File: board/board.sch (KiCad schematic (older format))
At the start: 47 parts, among them Q1 AO3401A, U1 STM32F405RGTx, U2 TPS542941, U3 MX25R3235FM2xx1, Y1 16MHz

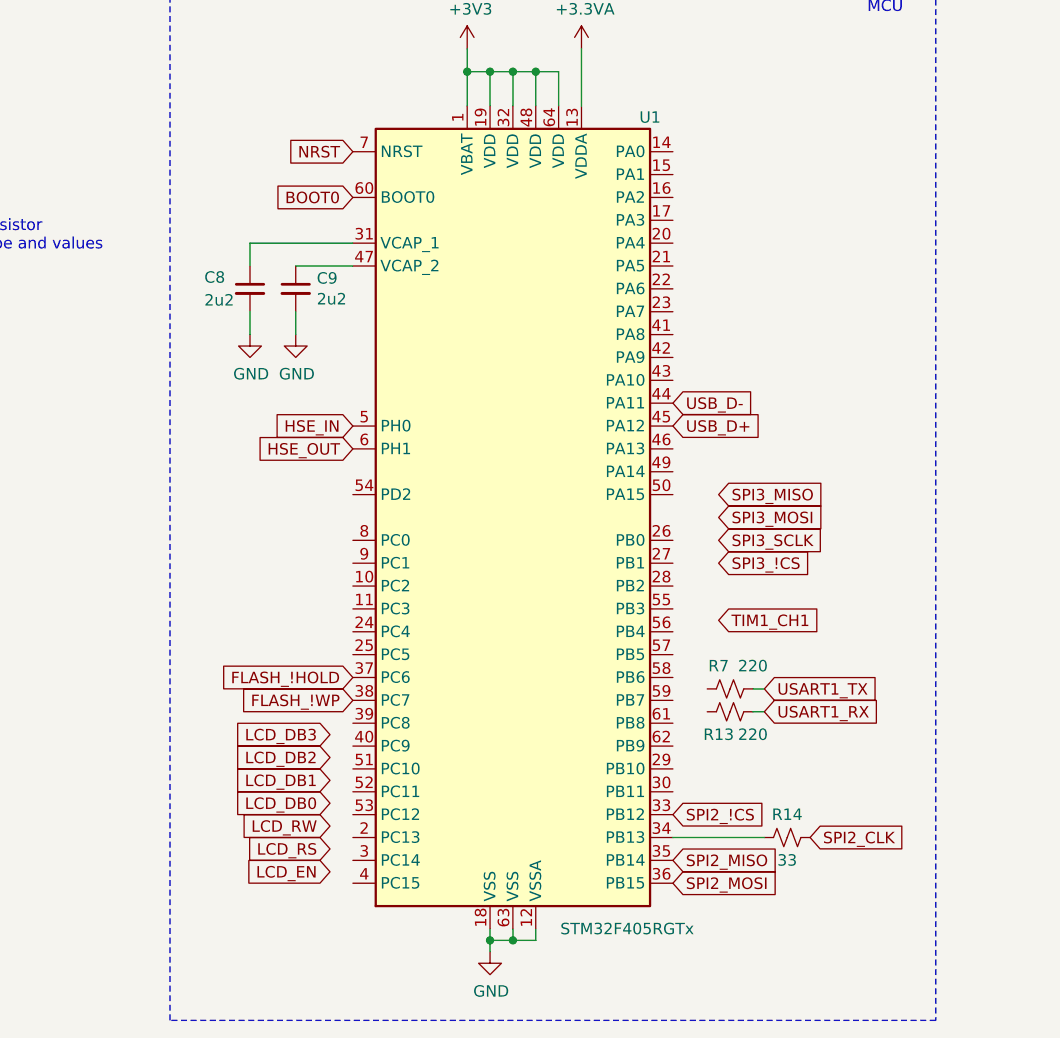
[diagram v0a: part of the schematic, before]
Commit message: Update on pinout
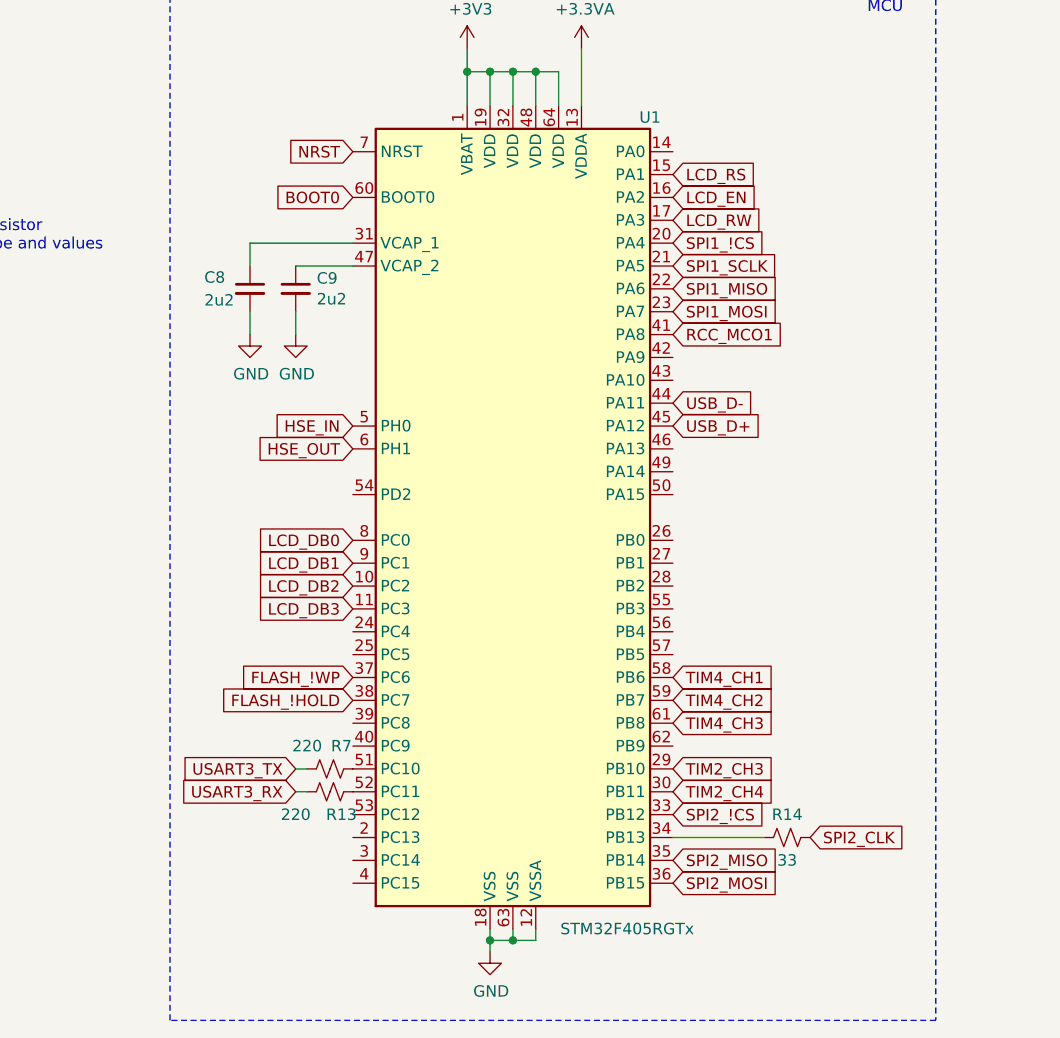
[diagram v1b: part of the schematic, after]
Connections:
- net FLASH_!HOLD: now also U1.38 (PC7); no longer U1.37 (PC6)
- net FLASH_!WP: now also U1.37 (PC6); no longer U1.38 (PC7)
- net LCD_DB0: now also U1.8 (PC0)
- net LCD_DB1: now also U1.9 (PC1)
- net LCD_DB2: now also U1.10 (PC2)
- net LCD_DB3: now also U1.11 (PC3)
- net LCD_EN: now also U1.16 (PA2)
- net LCD_RS: now also U1.15 (PA1)
- net LCD_RW: now also U1.17 (PA3)
- net SPI1_!CS: now reaches U1.20 (PA4)
- net SPI1_SCLK: now reaches U1.21 (PA5)
- net SPI1_MISO: now reaches U1.22 (PA6)
- net SPI1_MOSI: now reaches U1.23 (PA7)
- net TIM2_CH3: now reaches U1.29 (PB10)
- net TIM2_CH4: now reaches U1.30 (PB11)
- net RCC_MCO1: now reaches U1.41 (PA8)
- net at U1.51 (PC10): now also R7.2
- net at U1.52 (PC11): now also R13.2
- net TIM4_CH1: now reaches U1.58 (PB6)
- net TIM4_CH2: now reaches U1.59 (PB7)
- net TIM4_CH3: now reaches U1.61 (PB8)
- net USART1_RX renamed USART3_RX
- net USART1_TX renamed USART3_TX
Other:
- moved on the sheet: R13, R7
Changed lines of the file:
@@
 Text GLabel 4150 7000 2    50   Input ~ 0
 SPI2_MOSI
+Text GLabel 2750 6200 0    50   Input ~ 0
+FLASH_!HOLD
 Text GLabel 2750 6100 0    50   Input ~ 0
-FLASH_!HOLD
-Text GLabel 2750 6200 0    50   Input ~ 0
 FLASH_!WP
 Text GLabel 4150 6900 2    50   Input ~ 0
@@
 F1 "sensors.sch" 50
 $EndSheet
-Text GLabel 4350 5850 2    50   Input ~ 0
-TIM1_CH1
 $Sheet
 S 2950 -1250 1300 900
@@
 F1 "connectors.sch" 50
 $EndSheet
-Text GLabel 4350 5600 2    50   Input ~ 0
-SPI3_!CS
-Text GLabel 4350 5500 2    50   Input ~ 0
-SPI3_SCLK
-Text GLabel 4350 5400 2    50   Input ~ 0
-SPI3_MOSI
-Text GLabel 4350 5300 2    50   Input ~ 0
-SPI3_MISO
+Text GLabel 4150 4200 2    50   Input ~ 0
+SPI1_!CS
+Text GLabel 4150 4300 2    50   Input ~ 0
+SPI1_SCLK
+Text GLabel 4150 4500 2    50   Input ~ 0
+SPI1_MOSI
+Text GLabel 4150 4400 2    50   Input ~ 0
+SPI1_MISO
 Wire Notes Line
 	3700 600  3700 1500
 Wire Notes Line
 	5450 1500 5450 600
-Text GLabel 4550 6150 2    50   Input ~ 0
-USART1_TX
-Text GLabel 4550 6250 2    50   Input ~ 0
-USART1_RX
-Text GLabel 2650 6950 0    50   Input ~ 0
+Text GLabel 4150 4000 2    50   Input ~ 0
 LCD_EN
-Text GLabel 2650 6750 0    50   Input ~ 0
+Text GLabel 4150 4100 2    50   Input ~ 0
 LCD_RW
 $Comp
@@
 	1    0    0    -1
 $EndComp
-Text GLabel 2650 6650 0    50   Input ~ 0
+Text GLabel 2750 5500 0    50   Input ~ 0
 LCD_DB0
-Text GLabel 2650 6550 0    50   Input ~ 0
+Text GLabel 2750 5600 0    50   Input ~ 0
 LCD_DB1
-Text GLabel 2650 6450 0    50   Input ~ 0
+Text GLabel 2750 5700 0    50   Input ~ 0
 LCD_DB2
-Text GLabel 2650 6350 0    50   Input ~ 0
+Text GLabel 2750 5800 0    50   Input ~ 0
 LCD_DB3
-Text GLabel 2650 6850 0    50   Input ~ 0
+Text GLabel 4150 3900 2    50   Input ~ 0
 LCD_RS
 $Comp
@@
 	6700 2800 6700 6250
 Wire Notes Line
-	5300 3050 5300 7600
-Wire Notes Line
 	5300 7600 1950 7600
 Wire Notes Line
@@
 Text Notes 2800 700  0    50   ~ 0
 MCU PWR Decoupling\n
+NoConn ~ 9250 5600
+NoConn ~ 8400 5600
+Text GLabel 4150 6500 2    50   Input ~ 0
+TIM2_CH3
+Text GLabel 4150 6600 2    50   Input ~ 0
+TIM2_CH4
+Text GLabel 4150 6100 2    50   Input ~ 0
+TIM4_CH1
+Text GLabel 4150 6200 2    50   Input ~ 0
+TIM4_CH2
+Text GLabel 4150 6300 2    50   Input ~ 0
+TIM4_CH3
+Wire Wire Line
+	2500 6600 2550 6600
+Wire Wire Line
+	2500 6500 2550 6500
+$Comp
+L Device:R_Small_US R13
+U 1 1 60B24566
+P 2650 6600
+F 0 "R13" V 2550 6550 50  0000 C CNN
+F 1 "220" V 2550 6750 50  0000 C CNN
+F 2 "Resistor_SMD:R_0603_1608Metric" H 2650 6600 50  0001 C CNN
+F 3 "~" H 2650 6600 50  0001 C CNN
+	1    2650 6600
+	0    -1   -1   0
+$EndComp
 $Comp
 L Device:R_Small_US R7
 U 1 1 60B240EB
-P 4400 6150
-F 0 "R7" V 4300 6100 50  0000 C CNN
-F 1 "220" V 4300 6250 50  0000 C CNN
-F 2 "Resistor_SMD:R_0603_1608Metric" H 4400 6150 50  0001 C CNN
-F 3 "~" H 4400 6150 50  0001 C CNN
-	1    4400 6150
-	0    1    1    0
-$EndComp
-$Comp
-L Device:R_Small_US R13
-U 1 1 60B24566
-P 4400 6250
-F 0 "R13" V 4500 6200 50  0000 C CNN
-F 1 "220" V 4500 6350 50  0000 C CNN
-F 2 "Resistor_SMD:R_0603_1608Metric" H 4400 6250 50  0001 C CNN
-F 3 "~" H 4400 6250 50  0001 C CNN
-	1    4400 6250
-	0    1    1    0
-$EndComp
-Wire Wire Line
-	4550 6150 4500 6150
-Wire Wire Line
-	4550 6250 4500 6250
-NoConn ~ 9250 5600
-NoConn ~ 8400 5600
+P 2650 6500
+F 0 "R7" V 2750 6450 50  0000 C CNN
+F 1 "220" V 2750 6600 50  0000 C CNN
+F 2 "Resistor_SMD:R_0603_1608Metric" H 2650 6500 50  0001 C CNN
+F 3 "~" H 2650 6500 50  0001 C CNN
+	1    2650 6500
+	0    -1   -1   0
+$EndComp
+Wire Notes Line
+	5300 3050 5300 7600
+Text GLabel 2500 6600 0    50   Input ~ 0
+USART3_RX
+Text GLabel 2500 6500 0    50   Input ~ 0
+USART3_TX
+Text GLabel 4150 4600 2    50   Input ~ 0
+RCC_MCO1
 $EndSCHEMATC

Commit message: Updated schematic
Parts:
- removed C18: 100n, Capacitor_SMD:C_0402_1005Metric, symbol Device:C_Small
- removed R14: 33, Resistor_SMD:R_0603_1608Metric, symbol Device:R_Small_US
- removed R15, R3, R6: 10k, Resistor_SMD:R_0603_1608Metric, symbol Device:R_Small_US
- removed U3: MX25R3235FM2xx1, Package_SO:SOP-8_5.28x5.23mm_P1.27mm, symbol Memory_Flash:MX25R3235FM2xx1
- added C19: 10u, Capacitor_SMD:C_0603_1608Metric, symbol Device:C_Small
- added D2: LED_RGB, symbol Device:LED_RGB
- added Q2, Q3, Q4: Q_NMOS_GDS, symbol Device:Q_NMOS_GDS
- added R7: 220, Resistor_SMD:R_0603_1608Metric, symbol Device:R_Small_US
- added R8, R9: 120, Resistor_SMD:R_0603_1608Metric, symbol Device:R_Small_US
- renumbered C24 to C11, C25 to C12, C26 to C13, C11 to C14, C13 to C15, C14 to C16, C12 to C17, C15 to C18, C8 to C2, C16 to C20, C17 to C21, C19 to C22, C20 to C23, C21 to C24, C9 to C4, C2 to C5, C5 to C6, C4 to C7, C6 to C8, C7 to C9, R7 to R1, R8 to R10, R9 to R11, R13 to R2, R1 to R3, R2 to R4, R4 to R5, R5 to R6
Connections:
- net labels added: 12V_IN, SPI1_CLK
- net labels removed: +12V, SPI1_SCLK
- wire segments 141 -> 149
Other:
- note added: "Connectors"
- note added: "Flush Surveillance Concept"
- note added: "RGB"
- note added: "Sensors"
- note added: "UART series resistor\nDecoupling type and values"
- note removed: "Check if this is pull up or down"
- note removed: "Custom STM32 Board"
- note removed: "Ext. Flash"
- note removed: "UART series resistor\nDecoupling type and values\nLCD ??\nPower LED???"
- note removed: "Under construction"
- moved on the sheet: C1, C10, C11, C12, C13, C14, C15, C16, C17, C18, C2, C20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

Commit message: Updated schematic
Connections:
- net labels added: +12V
- net labels removed: 12V_IN
- wire segments 149 -> 150
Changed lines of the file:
@@
 Wire Notes Line
 	6200 650  4500 650
-Wire Wire Line
-	4850 2100 4900 2100
-Text GLabel 4850 2100 0    50   Input ~ 0
-12V_IN
 NoConn ~ 6200 4450
 NoConn ~ 7050 4450
@@
 Text Notes 1400 -1400 0    98   ~ 20
 Sensors
+$Comp
+L power:+12V #PWR?
+U 1 1 60B83527
+P 4800 1950
+F 0 "#PWR?" H 4800 1800 50  0001 C CNN
+F 1 "+12V" H 4815 2123 50  0000 C CNN
+F 2 "" H 4800 1950 50  0001 C CNN
+F 3 "" H 4800 1950 50  0001 C CNN
+	1    4800 1950
+	1    0    0    -1
+$EndComp
+Wire Wire Line
+	4800 1950 4800 2100
+Wire Wire Line
+	4800 2100 4900 2100
 $EndSCHEMATC

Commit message: Updated footprints
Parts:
- D2: footprint (none) -> LED_SMD:LED_RGB_1210
- Q2, Q3, Q4: footprint (none) -> Package_TO_SOT_SMD:SOT-23
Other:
- note added: "Find RGB\n"
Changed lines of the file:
@@
 F 0 "Q2" H 5400 6700 50  0000 L CNN
 F 1 "Q_NMOS_GDS" H 5100 6600 50  0000 L CNN
-F 2 "" H 5400 6650 50  0001 C CNN
+F 2 "Package_TO_SOT_SMD:SOT-23" H 5400 6650 50  0001 C CNN
 F 3 "~" H 5200 6550 50  0001 C CNN
 	1    5200 6550
@@
 F 0 "Q3" H 5804 6896 50  0000 L CNN
 F 1 "Q_NMOS_GDS" H 5804 6805 50  0000 L CNN
-F 2 "" H 5800 6950 50  0001 C CNN
+F 2 "Package_TO_SOT_SMD:SOT-23" H 5800 6950 50  0001 C CNN
 F 3 "~" H 5600 6850 50  0001 C CNN
 	1    5600 6850
@@
 F 0 "Q4" H 6250 6700 50  0000 L CNN
 F 1 "Q_NMOS_GDS" H 6250 6600 50  0000 L CNN
-F 2 "" H 6250 6650 50  0001 C CNN
+F 2 "Package_TO_SOT_SMD:SOT-23" H 6250 6650 50  0001 C CNN
 F 3 "~" H 6050 6550 50  0001 C CNN
 	1    6050 6550
@@
 	6150 5550 6100 5550
 $Comp
-L power:GND #PWR021
+L power:GND #PWR022
 U 1 1 60BEDB34
 P 6150 5550
-F 0 "#PWR021" H 6150 5300 50  0001 C CNN
+F 0 "#PWR022" H 6150 5300 50  0001 C CNN
 F 1 "GND" H 6155 5377 50  0000 C CNN
 F 2 "" H 6150 5550 50  0001 C CNN
@@
 	5700 5550 5700 5650
 $Comp
-L power:+3V3 #PWR019
+L power:+3V3 #PWR020
 U 1 1 60BE178F
 P 5700 5500
-F 0 "#PWR019" H 5700 5350 50  0001 C CNN
+F 0 "#PWR020" H 5700 5350 50  0001 C CNN
 F 1 "+3V3" H 5715 5673 50  0000 C CNN
 F 2 "" H 5700 5500 50  0001 C CNN
@@
 $EndComp
 $Comp
-L power:GND #PWR020
+L power:GND #PWR021
 U 1 1 60BE0B31
 P 5700 7200
-F 0 "#PWR020" H 5700 6950 50  0001 C CNN
+F 0 "#PWR021" H 5700 6950 50  0001 C CNN
 F 1 "GND" H 5850 7150 50  0000 C CNN
 F 2 "" H 5700 7200 50  0001 C CNN
@@
 F 0 "D2" V 5746 5520 50  0000 R CNN
 F 1 "LED_RGB" V 5655 5520 50  0000 R CNN
-F 2 "" H 5700 5800 50  0001 C CNN
+F 2 "LED_SMD:LED_RGB_1210" H 5700 5800 50  0001 C CNN
 F 3 "~" H 5700 5800 50  0001 C CNN
 	1    5700 5850
@@
 	5050 3200 5050 3250
 $Comp
-L power:GND #PWR023
+L power:GND #PWR024
 U 1 1 60B1C138
 P 7150 4950
-F 0 "#PWR023" H 7150 4700 50  0001 C CNN
+F 0 "#PWR024" H 7150 4700 50  0001 C CNN
 F 1 "GND" H 7000 4900 50  0000 C CNN
 F 2 "" H 7150 4950 50  0001 C CNN
@@
 VFB2
 $Comp
-L power:GND #PWR026
+L power:GND #PWR027
 U 1 1 60B00D4D
 P 8550 4400
-F 0 "#PWR026" H 8550 4150 50  0001 C CNN
+F 0 "#PWR027" H 8550 4150 50  0001 C CNN
 F 1 "GND" H 8555 4227 50  0000 C CNN
 F 2 "" H 8550 4400 50  0001 C CNN
@@
 EN2_IN
 $Comp
-L power:GND #PWR024
+L power:GND #PWR025
 U 1 1 60AF4CB3
 P 8400 3600
-F 0 "#PWR024" H 8400 3350 50  0001 C CNN
+F 0 "#PWR025" H 8400 3350 50  0001 C CNN
 F 1 "GND" H 8405 3427 50  0000 C CNN
 F 2 "" H 8400 3600 50  0001 C CNN
@@
 PGND1
 $Comp
-L power:GND #PWR016
+L power:GND #PWR017
 U 1 1 60A75B9C
 P 5250 3550
-F 0 "#PWR016" H 5250 3300 50  0001 C CNN
+F 0 "#PWR017" H 5250 3300 50  0001 C CNN
 F 1 "GND" H 5255 3377 50  0000 C CNN
 F 2 "" H 5250 3550 50  0001 C CNN
@@
 $EndComp
 $Comp
-L power:GND #PWR013
+L power:GND #PWR014
 U 1 1 60A78713
 P 5050 4150
-F 0 "#PWR013" H 5050 3900 50  0001 C CNN
+F 0 "#PWR014" H 5050 3900 50  0001 C CNN
 F 1 "GND" H 5055 3977 50  0000 C CNN
 F 2 "" H 5050 4150 50  0001 C CNN
@@
 $EndComp
 $Comp
-L power:+5V #PWR012
+L power:+5V #PWR013
 U 1 1 60A6D9C0
 P 5050 3200
-F 0 "#PWR012" H 5050 3050 50  0001 C CNN
+F 0 "#PWR013" H 5050 3050 50  0001 C CNN
 F 1 "+5V" H 5065 3373 50  0000 C CNN
 F 2 "" H 5050 3200 50  0001 C CNN
@@
 $EndComp
 $Comp
-L power:+3V3 #PWR025
+L power:+3V3 #PWR026
 U 1 1 60A69F8C
 P 8550 3200
-F 0 "#PWR025" H 8550 3050 50  0001 C CNN
+F 0 "#PWR026" H 8550 3050 50  0001 C CNN
 F 1 "+3V3" H 8565 3373 50  0000 C CNN
 F 2 "" H 8550 3200 50  0001 C CNN
@@
 $EndComp
 $Comp
-L power:GND #PWR014
+L power:GND #PWR015
 U 1 1 6090B6B1
 P 5100 2400
-F 0 "#PWR014" H 5100 2150 50  0001 C CNN
+F 0 "#PWR015" H 5100 2150 50  0001 C CNN
 F 1 "GND" H 5105 2227 50  0000 C CNN
 F 2 "" H 5100 2400 50  0001 C CNN
@@
 $EndComp
 $Comp
-L power:GND #PWR022
+L power:GND #PWR023
 U 1 1 60910D18
 P 6300 2300
-F 0 "#PWR022" H 6300 2050 50  0001 C CNN
+F 0 "#PWR023" H 6300 2050 50  0001 C CNN
 F 1 "GND" H 6305 2127 50  0000 C CNN
 F 2 "" H 6300 2300 50  0001 C CNN
@@
 	6200 1550 6200 650
 $Comp
-L power:GND #PWR018
+L power:GND #PWR019
 U 1 1 60A3071E
 P 5600 1250
-F 0 "#PWR018" H 5600 1000 50  0001 C CNN
+F 0 "#PWR019" H 5600 1000 50  0001 C CNN
 F 1 "GND" H 5605 1077 50  0000 C CNN
 F 2 "" H 5600 1250 50  0001 C CNN
@@
 $EndComp
 $Comp
-L power:GND #PWR015
+L power:GND #PWR016
 U 1 1 60A2FFCD
 P 5200 1250
-F 0 "#PWR015" H 5200 1000 50  0001 C CNN
+F 0 "#PWR016" H 5200 1000 50  0001 C CNN
 F 1 "GND" H 5205 1077 50  0000 C CNN
 F 2 "" H 5200 1250 50  0001 C CNN
@@
 	5600 950  5600 1050
 $Comp
-L power:+3.3VA #PWR017
+L power:+3.3VA #PWR018
 U 1 1 60A2600F
 P 5600 950
-F 0 "#PWR017" H 5600 800 50  0001 C CNN
+F 0 "#PWR018" H 5600 800 50  0001 C CNN
 F 1 "+3.3VA" H 5615 1123 50  0000 C CNN
 F 2 "" H 5600 950 50  0001 C CNN
@@
 Sensors
 $Comp
-L power:+12V #PWR?
+L power:+12V #PWR012
 U 1 1 60B83527
 P 4800 1950
-F 0 "#PWR?" H 4800 1800 50  0001 C CNN
+F 0 "#PWR012" H 4800 1800 50  0001 C CNN
 F 1 "+12V" H 4815 2123 50  0000 C CNN
 F 2 "" H 4800 1950 50  0001 C CNN
@@
 Wire Wire Line
 	4800 2100 4900 2100
+Text Notes 6650 5550 0    98   ~ 20
+Find RGB\n
 $EndSCHEMATC

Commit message: Updated layout
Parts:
- removed Q1: AO3401A, Package_TO_SOT_SMD:SOT-23, symbol Transistor_FET:AO3401A
- removed R1, R2: 220, Resistor_SMD:R_0603_1608Metric, symbol Device:R_Small_US
- removed U1: STM32F405RGTx, Package_QFP:LQFP-64_10x10mm_P0.5mm, symbol MCU_ST_STM32F4:STM32F405RGTx
- added U?: STM32F405RGTx, Package_QFP:LQFP-64_10x10mm_P0.5mm, symbol MCU_ST_STM32F4:STM32F405RGTx
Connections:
- wire segments 150 -> 147
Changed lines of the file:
@@
 Flush Surveillance Concept
-$Comp
-L MCU_ST_STM32F4:STM32F405RGTx U1
-U 1 1 608D985A
-P 2400 4000
-F 0 "U1" H 3000 5750 50  0000 C CNN
-F 1 "STM32F405RGTx" H 2900 2200 50  0000 C CNN
-F 2 "Package_QFP:LQFP-64_10x10mm_P0.5mm" H 1800 2300 50  0001 R CNN
-F 3 "http://www.st.com/st-web-ui/static/active/en/resource/technical/document/datasheet/DM00037051.pdf" H 2400 4000 50  0001 C CNN
-	1    2400 4000
-	1    0    0    -1
-$EndComp
 $Comp
 L power:+3V3 #PWR06
@@
 Text GLabel 3100 4900 2    50   Input ~ 0
 TIM4_CH3
-Wire Wire Line
-	1450 5200 1500 5200
-Wire Wire Line
-	1450 5100 1500 5100
-$Comp
-L Device:R_Small_US R2
-U 1 1 60B24566
-P 1600 5200
-F 0 "R2" V 1500 5150 50  0000 C CNN
-F 1 "220" V 1500 5350 50  0000 C CNN
-F 2 "Resistor_SMD:R_0603_1608Metric" H 1600 5200 50  0001 C CNN
-F 3 "~" H 1600 5200 50  0001 C CNN
-	1    1600 5200
-	0    -1   -1   0
-$EndComp
-$Comp
-L Device:R_Small_US R1
-U 1 1 60B240EB
-P 1600 5100
-F 0 "R1" V 1700 5050 50  0000 C CNN
-F 1 "220" V 1700 5200 50  0000 C CNN
-F 2 "Resistor_SMD:R_0603_1608Metric" H 1600 5100 50  0001 C CNN
-F 3 "~" H 1600 5100 50  0001 C CNN
-	1    1600 5100
-	0    -1   -1   0
-$EndComp
-Text GLabel 1450 5200 0    50   Input ~ 0
-USART3_RX
-Text GLabel 1450 5100 0    50   Input ~ 0
-USART3_TX
 Text GLabel 3100 3200 2    50   Input ~ 0
 RCC_MCO1
@@
 Wire Wire Line
 	5700 2100 5850 2100
-Wire Wire Line
-	5300 2100 5500 2100
 $Comp
 L board-rescue:TPS542941 U2
@@
 $EndComp
 $Comp
-L Transistor_FET:AO3401A Q1
-U 1 1 60907C55
-P 5100 2200
-F 0 "Q1" V 5442 2200 50  0000 C CNN
-F 1 "AO3401A" V 5351 2200 50  0000 C CNN
-F 2 "Package_TO_SOT_SMD:SOT-23" H 5300 2125 50  0001 L CIN
-F 3 "http://www.aosmd.com/pdfs/datasheet/AO3401A.pdf" H 5100 2200 50  0001 L CNN
-	1    5100 2200
-	0    -1   -1   0
-$EndComp
-$Comp
-L power:GND #PWR015
-U 1 1 6090B6B1
-P 5100 2400
-F 0 "#PWR015" H 5100 2150 50  0001 C CNN
-F 1 "GND" H 5105 2227 50  0000 C CNN
-F 2 "" H 5100 2400 50  0001 C CNN
-F 3 "" H 5100 2400 50  0001 C CNN
-	1    5100 2400
-	1    0    0    -1
-$EndComp
-$Comp
 L Device:Ferrite_Bead_Small FB2
 U 1 1 6090BE99
@@
 Wire Wire Line
 	4800 1950 4800 2100
-Wire Wire Line
-	4800 2100 4900 2100
 Text Notes 6650 5550 0    98   ~ 20
 Find RGB\n
+Text GLabel 1700 5100 0    50   Input ~ 0
+USART3_TX
+Text GLabel 1700 5200 0    50   Input ~ 0
+USART3_RX
+$Comp
+L MCU_ST_STM32F4:STM32F405RGTx U?
+U 1 1 60C86C3C
+P 2400 4000
+F 0 "U?" H 2850 5800 50  0000 C CNN
+F 1 "STM32F405RGTx" H 2950 2150 50  0000 C CNN
+F 2 "Package_QFP:LQFP-64_10x10mm_P0.5mm" H 1800 2300 50  0001 R CNN
+F 3 "http://www.st.com/st-web-ui/static/active/en/resource/technical/document/datasheet/DM00037051.pdf" H 2400 4000 50  0001 C CNN
+	1    2400 4000
+	1    0    0    -1
+$EndComp
+Wire Wire Line
+	4800 2100 5500 2100
 $EndSCHEMATC
